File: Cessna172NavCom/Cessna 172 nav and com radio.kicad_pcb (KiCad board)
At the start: 2 copper layers, 180 x 98 mm, 95 parts, among them J1 EN11-HSM1BF20, J2 USB_B_Micro, J3 EN11-HSM1BF20, J4 EN11-HSM1BF20, J5 EN11-HSM1BF20, J6 EN11-HSM1BF20, J7 EN11-HSM1BF20, J8 Conn_02x20_Odd_Even, SW1 SW_Push, SW2 SW_Push, SW3 SW_Push, SW4 SW_Push, SW5 SW_Push, SW6 SW_Push, U1 MAX7219 COM standby, U10 3651A, U11 MAX7219 COM standby, U12 3651A, U13 MAX7219 COM standby, U14 3651A, U15 MAX7219 COM standby, U16 3651A, U2 3651A, U3 MAX7219 COM standby, U4 3651A, U5 MAX7219 COM standby, U6 3651A, U7 MAX7219 COM standby, U8 3651A, U9 MAX7219 COM standby

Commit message: Fully routed woot woot!
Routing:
- net GND: track 0.00 -> 799.6 mm, vias 0 -> 1
- net +5V: track 0.00 -> 595.3 mm, vias 0 -> 5
- net CLK: track 0.00 -> 438.1 mm, vias 0 -> 7
- net LOAD: track 0.00 -> 400.2 mm, vias 0 -> 5
- net ISET: track 0.00 -> 349.0 mm, vias 0 -> 8
- net DIN: track 0.00 -> 177.3 mm, vias 0 -> 1
- net TEST2_SW: track 0.00 -> 174.9 mm
- net COMM2_VOL_LEFT: track 0.00 -> 174.8 mm, vias 0 -> 1
- net TEST1_SW: track 0.00 -> 169.1 mm
- net COMM2_VOL_RIGHT: track 0.00 -> 168.3 mm, vias 0 -> 1
- net COMM1_VOL_RIGHT: track 0.00 -> 162.4 mm, vias 0 -> 1
- net COMM2_TX_SW: track 0.00 -> 153.8 mm, vias 0 -> 2
- net /sheet5F68A9C2/DIN: track 0.00 -> 152.0 mm, vias 0 -> 2
- net COMM1_VOL_LEFT: track 0.00 -> 146.2 mm, vias 0 -> 1
- net COMM2_LEFT: track 0.00 -> 142.1 mm, vias 0 -> 1
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
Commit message: Fully routed!!!
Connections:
- J8 pad 27: Net-(J8-Pad27) -> GND
- J8 pad 28: Net-(J8-Pad28) -> GND
- J8 pad 29: Net-(J8-Pad29) -> GND
- J8 pad 30: Net-(J8-Pad30) -> GND
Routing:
- net GND: track 799.6 -> 217.1 mm, vias 1 -> 101
- net CHAN1_LED: track 128.9 -> 129.3 mm, vias 2 -> 3
- net +5V: vias 5 -> 6
- net COMM2_VOL_RIGHT: vias 1 -> 2
- net /sheet5F71BCD3/B1: vias 0 -> 1
- added copper zone on B.Cu, net GND
- added copper zone on F.Cu, net GND
- removed copper zone on B.Cu, net (none)
- removed copper zone on F.Cu, net (none)

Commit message: Minor PCB cleanup
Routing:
- net GND: track 217.1 -> 215.1 mm, vias 101 -> 100
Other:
- board text removed: "180x38"

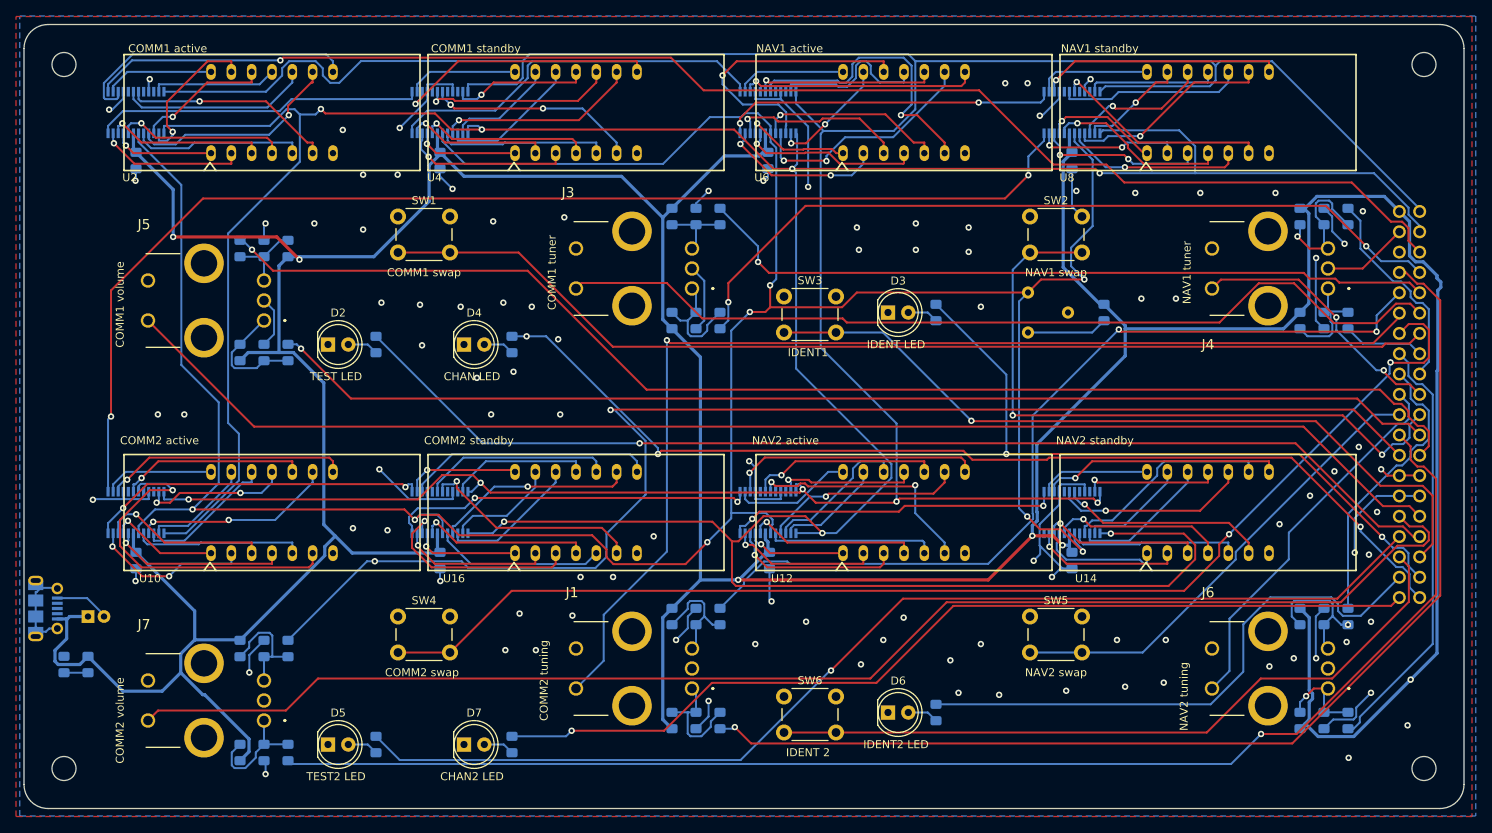
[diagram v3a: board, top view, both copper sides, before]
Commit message: Remove unnecessary items, rename some of the nets
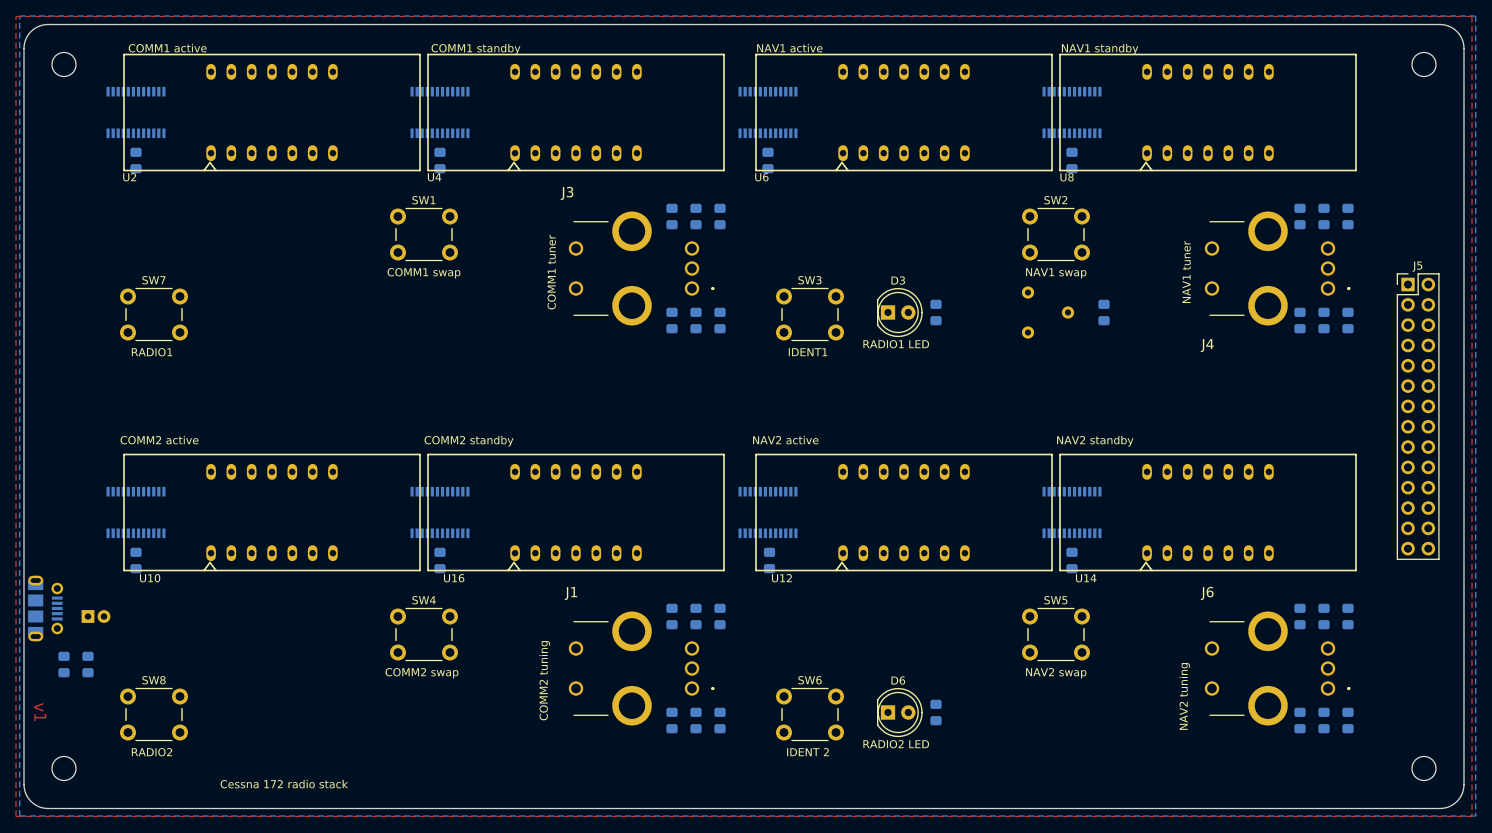
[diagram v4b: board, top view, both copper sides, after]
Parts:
- removed C10, C11, C20, C21: 0.1uf, Capacitor_SMD:C_0805_2012Metric_Pad1.15x1.40mm_HandSolder
- removed D2, D4, D5, D7: LED, LED_THT:LED_D5.0mm
- removed J7: EN11-HSM1BF20, SamacSys_Parts:EN11HSM1BF20
- removed J8: Conn_02x20_Odd_Even, SamacSys_Parts:SAMTEC-TST-120-01-X-D
- removed R13, R14, R15, R16, R29, R30, R31, R32: 10k, Resistor_SMD:R_0805_2012Metric_Pad1.15x1.40mm_HandSolder
- removed R17, R18, R20, R3: 220k, Resistor_SMD:R_0805_2012Metric_Pad1.15x1.40mm_HandSolder
- added SW7: SW_Push, Button_Switch_THT:SW_PUSH_6mm_H8mm, F.Cu at (43.0, 64.0)
- added SW8: SW_Push, Button_Switch_THT:SW_PUSH_6mm_H8mm, F.Cu at (43.0, 114.0)
- J5: value EN11-HSM1BF20 -> Conn_02x14_Odd_Even; footprint SamacSys_Parts:EN11HSM1BF20 -> Connector_PinHeader_2.54mm:PinHeader_2x14_P2.54mm_Vertical
- moved J5 143.1 mm to (203.0, 62.5), turned to 0 degrees
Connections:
- R19 pad 2: IDENT2_LED -> RADIO2_LED
- R4 pad 2: IDENT1_LED -> RADIO1_LED
- SW1 pad 2: COMM1_TX_SW -> COMM1_XFR
- SW2 pad 2: NAV1_TX_SW -> NAV1_XFR
- SW4 pad 2: COMM2_TX_SW -> COMM2_XFR
- SW5 pad 2: NAV2_TX_SW -> NAV2_XFR
- U1 pad 12: LOAD -> CS_LOAD
- U11 pad 12: LOAD -> CS_LOAD
- U13 pad 12: LOAD -> CS_LOAD
- U15 pad 12: LOAD -> CS_LOAD
- U3 pad 12: LOAD -> CS_LOAD
- U5 pad 12: LOAD -> CS_LOAD
- U7 pad 12: LOAD -> CS_LOAD
- U9 pad 12: LOAD -> CS_LOAD
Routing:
- net +5V: track 595.3 -> 0.00 mm, vias 6 -> 0
- net CLK: track 438.1 -> 0.00 mm, vias 7 -> 0
- net LOAD: track 400.2 -> 0.00 mm, vias 5 -> 0
- net ISET: track 349.0 -> 0.00 mm, vias 8 -> 0
- net GND: track 215.1 -> 0.00 mm, vias 100 -> 0
- net DIN: track 177.3 -> 0.00 mm, vias 1 -> 0
- net TEST2_SW: track 174.9 -> 0.00 mm
- net COMM2_VOL_LEFT: track 174.8 -> 0.00 mm, vias 1 -> 0
- net TEST1_SW: track 169.1 -> 0.00 mm
- net COMM2_VOL_RIGHT: track 168.3 -> 0.00 mm, vias 2 -> 0
- net COMM1_VOL_RIGHT: track 162.4 -> 0.00 mm, vias 1 -> 0
- net COMM2_TX_SW: track 153.8 -> 0.00 mm, vias 2 -> 0
- net /sheet5F68A9C2/DIN: track 152.0 -> 0.00 mm, vias 2 -> 0
- net COMM1_VOL_LEFT: track 146.2 -> 0.00 mm, vias 1 -> 0
- net COMM2_LEFT: track 142.1 -> 0.00 mm, vias 1 -> 0
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- added copper zone on B.Cu, net (none)
- removed copper zone on B.Cu, net GND
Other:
- board text added: "Cessna 172 radio stack"
- board text added: "RADIO1"
- board text added: "RADIO1 LED"
- board text added: "RADIO2"
- board text added: "RADIO2 LED"
- board text added: "v1"
- board text removed: "CHAN LED"
- board text removed: "CHAN2 LED"
- board text removed: "COMM1 volume"
- board text removed: "COMM2 volume"
- board text removed: "IDENT LED"
- board text removed: "IDENT2 LED"
- board text removed: "TEST LED"
- board text removed: "TEST2 LED"

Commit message: Switch to 30 pin connector for availability reasons
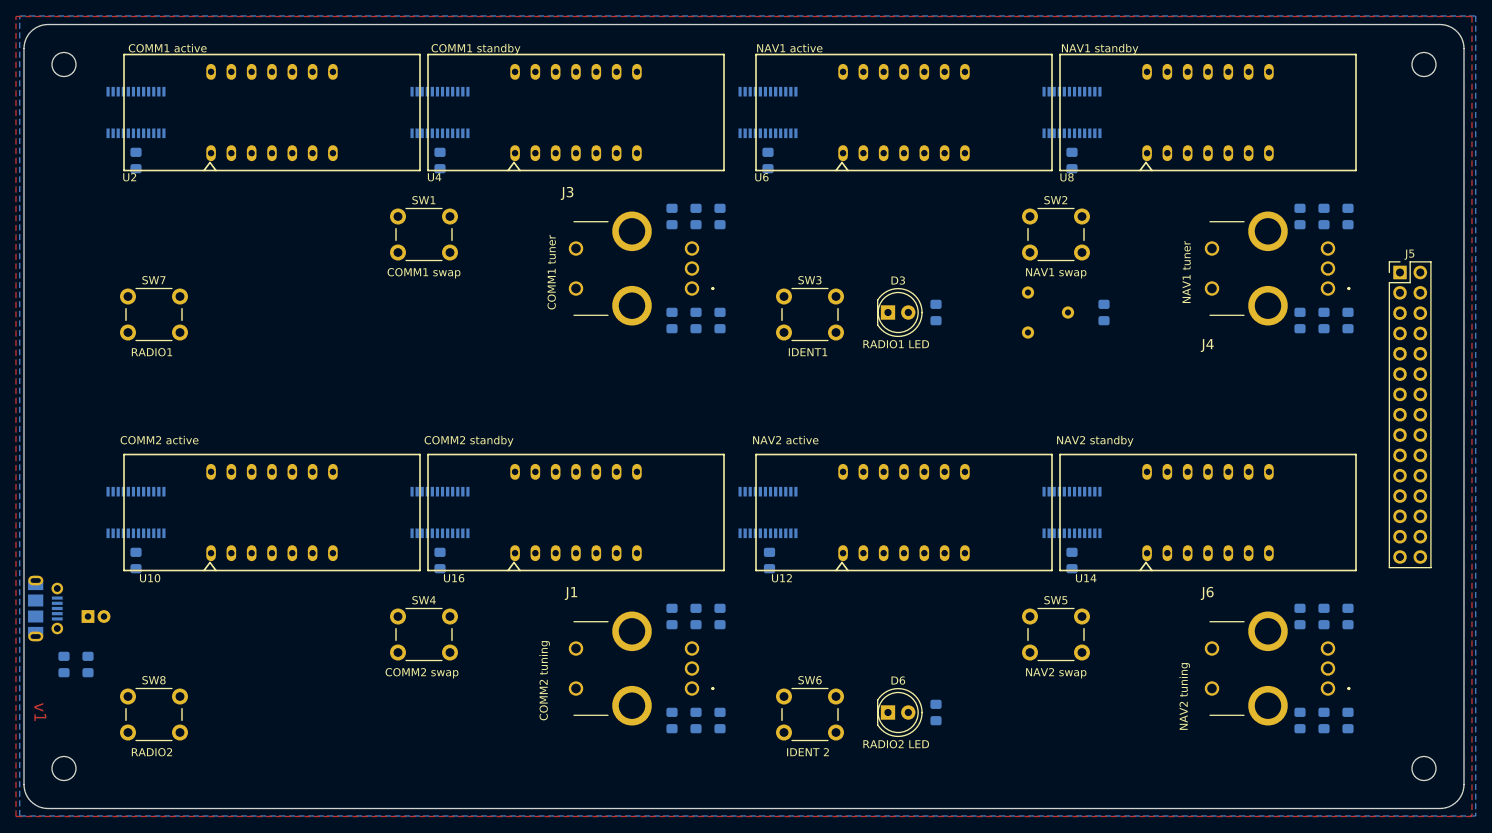
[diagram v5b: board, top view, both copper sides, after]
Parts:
- J5: value Conn_02x14_Odd_Even -> Conn_02x15_Odd_Even; footprint Connector_PinHeader_2.54mm:PinHeader_2x14_P2.54mm_Vertical -> Connector_PinHeader_2.54mm:PinHeader_2x15_P2.54mm_Vertical
- moved J5 1.80 mm to (202.0, 61.0)
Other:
- board text added: "1"
- board text added: "2"
- board text added: "29"
- board text added: "30"

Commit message: Arduino shield plus more main board changes
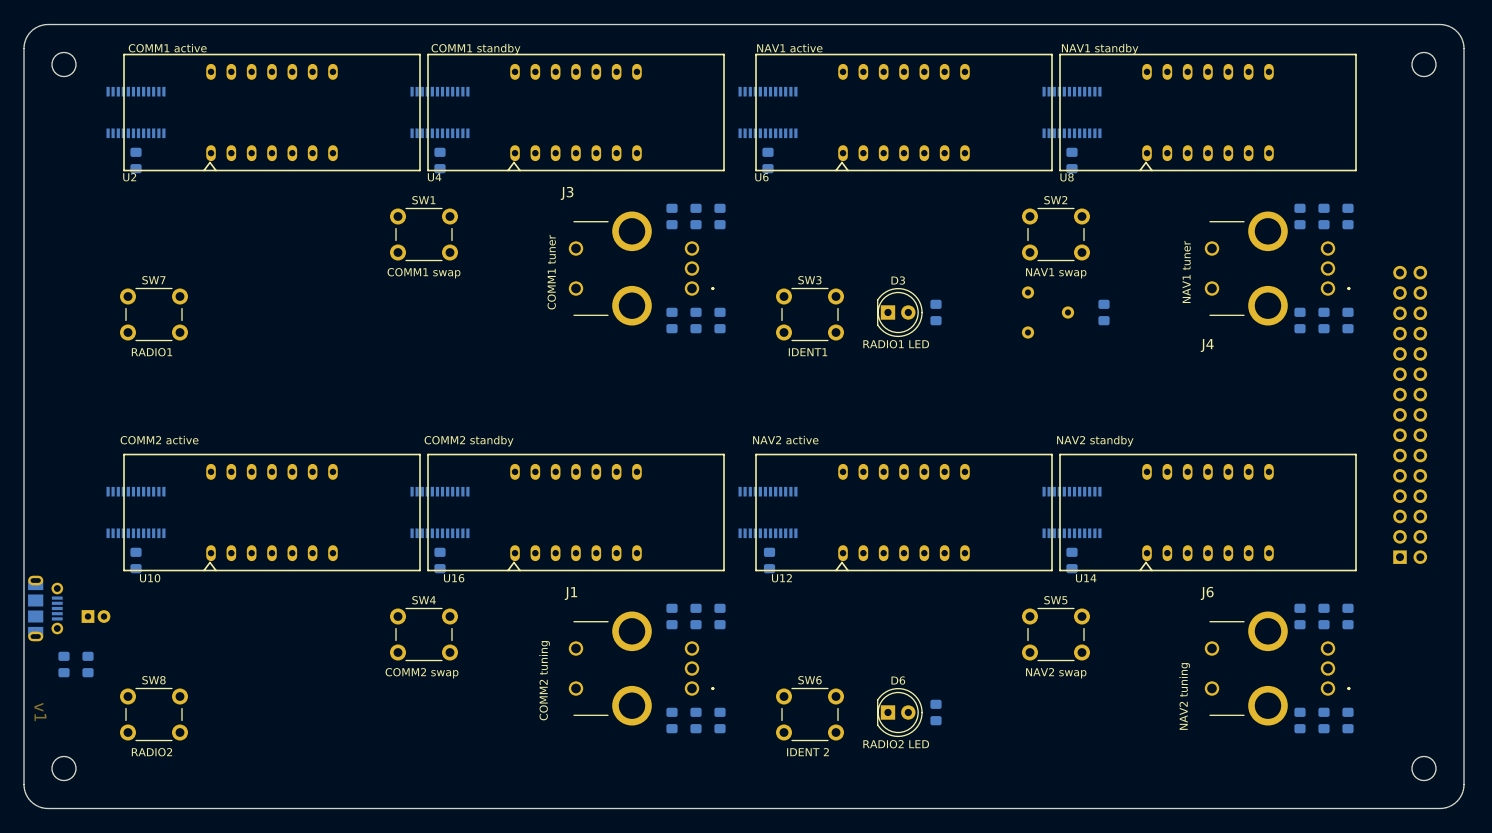
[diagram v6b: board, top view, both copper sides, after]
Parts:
- J5: moved to B.Cu
- moved J5 35.6 mm to (202.0, 96.6)
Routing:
- removed copper zone on B.Cu, net (none)
- removed copper zone on F.Cu, net GND

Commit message: Added autoroute and pour
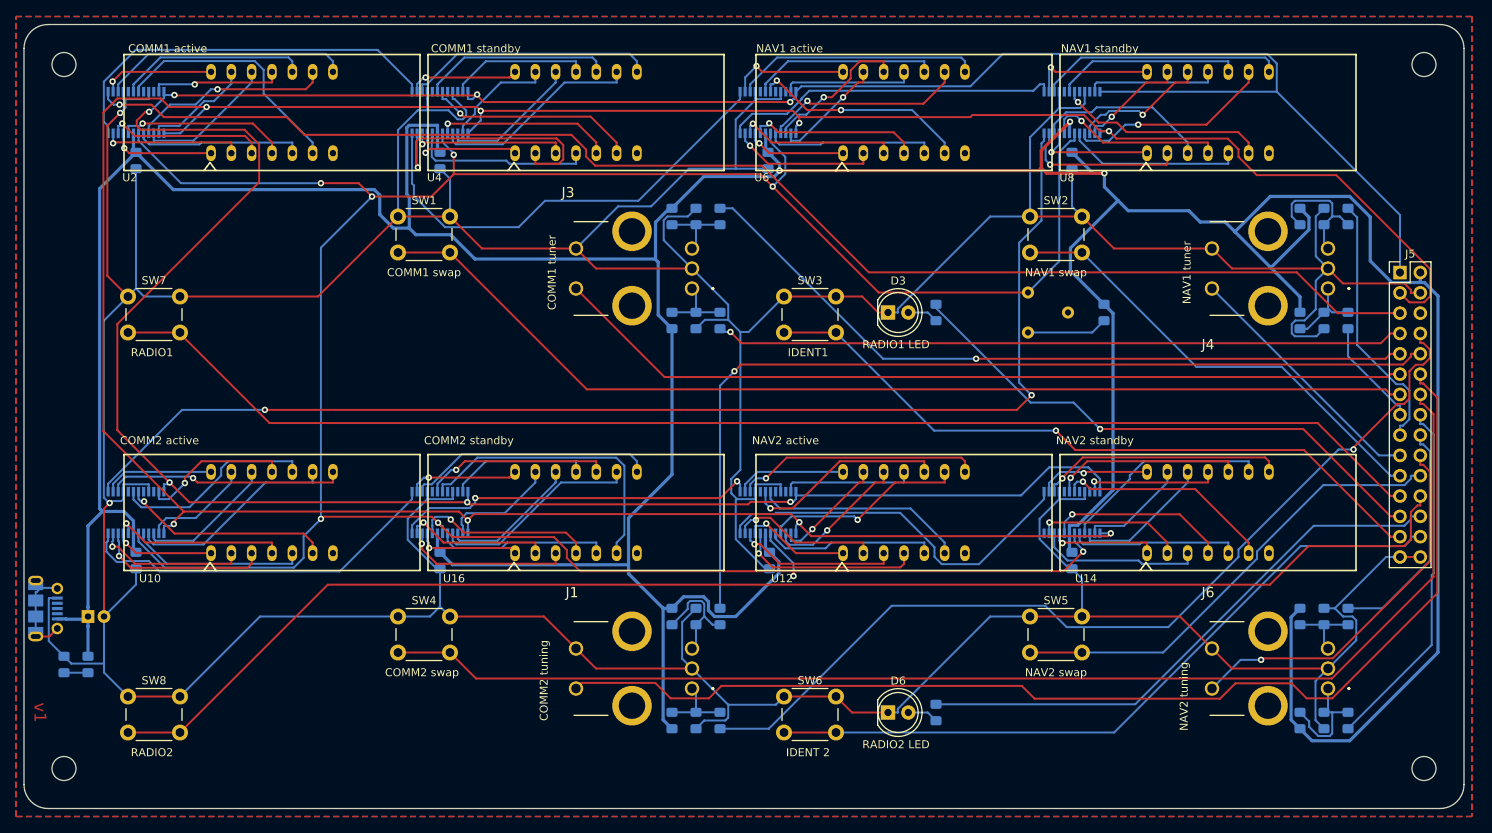
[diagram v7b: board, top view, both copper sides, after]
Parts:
- J5: moved to F.Cu
- moved J5 35.6 mm to (202.0, 61.0)
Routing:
- net GND: track 0.00 -> 764.2 mm, vias 0 -> 2
- net +5V: track 0.00 -> 586.3 mm, vias 0 -> 3
- net CS_LOAD: track 0.00 -> 400.0 mm, vias 0 -> 7
- net CLK: track 0.00 -> 378.8 mm, vias 0 -> 8
- net ISET: track 0.00 -> 342.2 mm, vias 0 -> 8
- net RADIO2_SW: track 0.00 -> 176.5 mm
- net DIN: track 0.00 -> 174.0 mm, vias 0 -> 1
- net RADIO1_SW: track 0.00 -> 167.5 mm
- net COMM2_XFR: track 0.00 -> 159.8 mm
- net /sheet5F68A9C2/DIN: track 0.00 -> 155.7 mm, vias 0 -> 2
- net COMM2_KHZ_SW: track 0.00 -> 145.6 mm
- net COMM1_XFR: track 0.00 -> 132.6 mm
- net COMM2_RIGHT: track 0.00 -> 117.2 mm, vias 0 -> 1
- net COMM2_LEFT: track 0.00 -> 116.6 mm, vias 0 -> 1
- net COMM1_KHZ_SW: track 0.00 -> 107.7 mm
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- added copper zone on F.Cu, net (none)
- added copper zone on B.Cu, net GND
- added copper zone on F.Cu, net GND

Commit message: Re-routed with new LED position
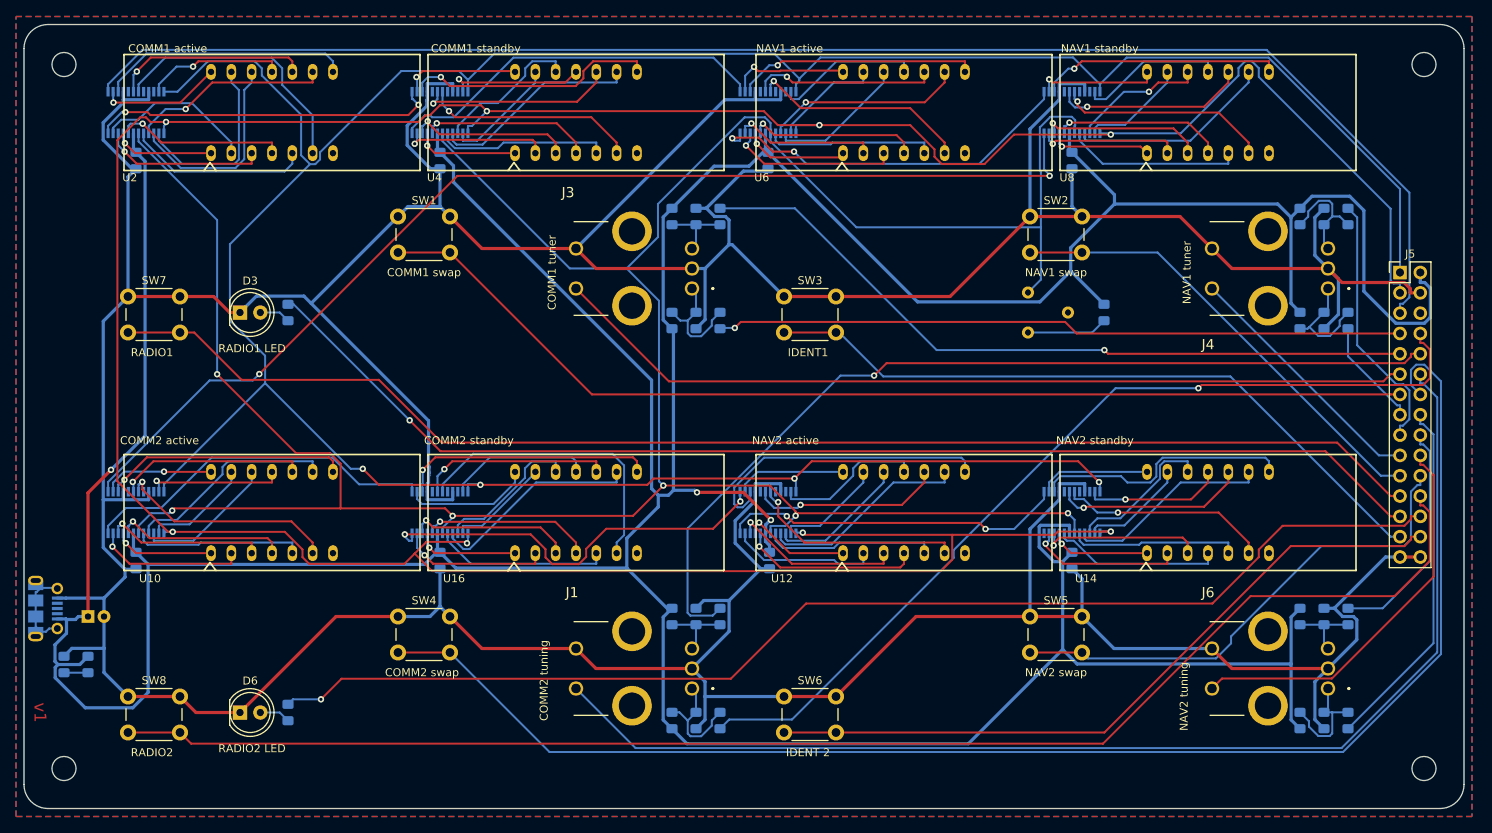
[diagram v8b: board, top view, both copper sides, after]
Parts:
- moved D3 81.0 mm to (57.0, 66.0)
- moved D6 81.0 mm to (57.0, 116.0)
- moved R19 81.0 mm to (63.0, 116.0)
- moved R4 81.0 mm to (63.0, 66.0)
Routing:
- net RADIO2_LED: track 70.5 -> 152.0 mm, vias 0 -> 1
- net RADIO1_LED: track 69.2 -> 150.0 mm
- net CS_LOAD: track 400.0 -> 368.1 mm, vias 7 -> 4
- net CLK: track 378.8 -> 409.4 mm
- net +5V: track 586.3 -> 614.6 mm
- net GND: track 764.2 -> 737.4 mm, vias 2 -> 0
- net COMM2_XFR: track 159.8 -> 183.1 mm
- net /sheet5F68A9C2/DIN: track 155.7 -> 140.4 mm
- net /sheet5F611637/SEG_D: track 33.4 -> 18.2 mm
- net DIN: track 174.0 -> 188.5 mm, vias 1 -> 0
- net /sheet5F613960/DIN: track 57.9 -> 47.8 mm
- net /5 digit LCD display/SEG_A: track 13.7 -> 23.7 mm
- net /5 digit LCD display/SEG_F: track 17.5 -> 25.4 mm
- net /sheet5F68A9C3/DIG_4: track 30.7 -> 37.5 mm, vias 1 -> 0
- net ISET: track 342.2 -> 348.8 mm, vias 8 -> 6
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- removed copper zone on F.Cu, net (none)
